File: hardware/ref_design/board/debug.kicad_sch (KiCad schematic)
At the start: 6 parts, among them J5 SWD, J6 UART, SW18 BOOTSEL, SW19 RESET

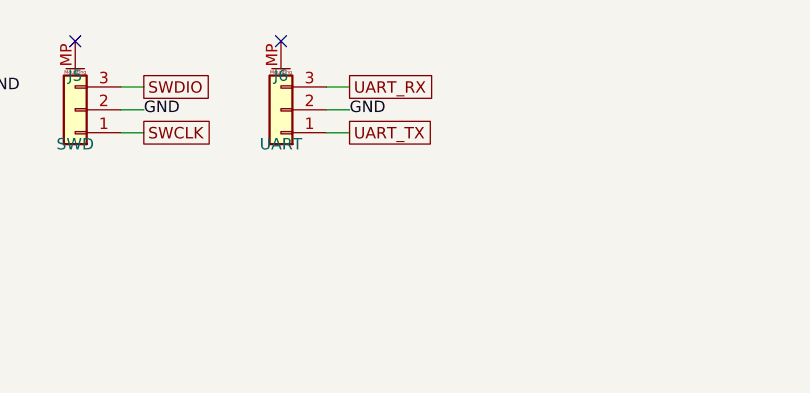
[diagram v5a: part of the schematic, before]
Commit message: Reference design: checklist changes and the datasheet pin gate
Board: PWR_HOLD pull-down (R42, also covers RP2350-E9), charge current
3.3k (333-364 mA), firmware charge pause (CHG_OFF, Q4), R13 33k, 0.1 ohm
in D5's path, JP1/JP2 cut-jumpers, TP6-8, spare 1206 footprints, 4-bit
revision strap on GPIO22-25 (REV 1 on the back).

Datasheet review of every part's pins (pin_review/, tools/check_pins.py)
found and fixed: J6 TX/RX swapped against Raspberry Pi's debug connector
spec, USB series resistors 22 to 27 ohm, the ME6211 CE able to lead its
VIN at a live plug-in (C47 on PWR_EN).

Case: silicone height 1.2 mm from the DS Lite, chamfered step.

Co-Authored-By: Claude Opus 5.5 <noreply@anthropic.com>
Claude-Session: https://claude.ai/code/session_01MUt6paNsT75sqwAr83zRS3
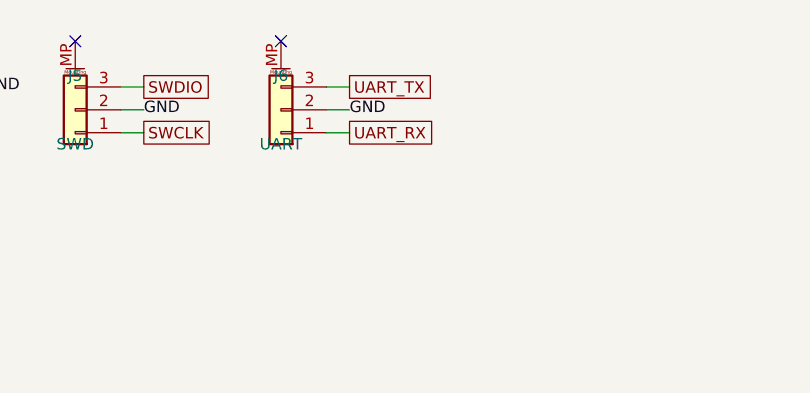
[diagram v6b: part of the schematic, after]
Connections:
- net UART_RX: now also J6.1 (Pin_1); no longer J6.3 (Pin_3)
- net UART_TX: now also J6.3 (Pin_3); no longer J6.1 (Pin_1)
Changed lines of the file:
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@@
     (at 170.18 33.02 0)
+)
+  (global_label "UART_TX"
+    (shape passive)
+    (at 193.04 27.94 0)
 )
   (global_label "UART_RX"
     (shape passive)
-    (at 193.04 27.94 0)
-)
-  (global_label "UART_TX"
-    (shape passive)
     (at 193.04 33.02 0)
